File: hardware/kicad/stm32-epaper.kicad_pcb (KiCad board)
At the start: 4 copper layers, 97.4 x 60 mm, 155 parts, among them J1 USB_C_Receptacle_USB2.0_16P, J101 TC2050-IDC-NL, J102 UART (TX RX GND), J2 BATT (1S LiPo), J201 microSD, J301 IT8951 HAT, J302 Electrodes L, J303 Electrodes R, SW101 BOOT, SW301 PEC11R-4220F-S0024, SW302 POWER, U1 BQ24073RGT, U101 STM32F469IIT6, U2 TPS63802DLA, U201 IS42S16400J-6TLI, U202 W25Q128JVSIQ, U3 TPS61023DRL, U301 CAP1188-1-CP-TR, U302 TPD4E05U06DQAR, U4 TPS22965DSG, U5 USBLC6-2SC6, U6 TPS63900DSK, U7 MCP1700T-3002E/TT, Y101 8MHz CL8pF, Y102 32.768kHz CL6pF

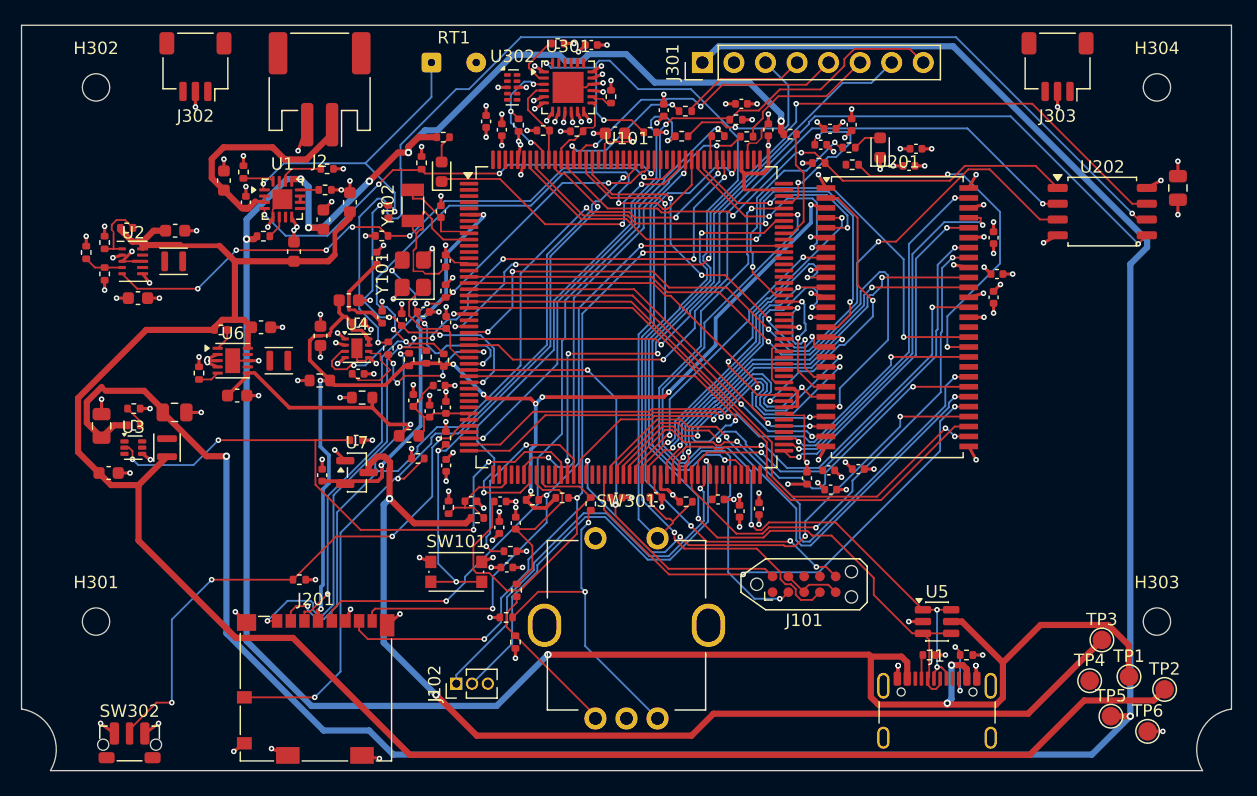
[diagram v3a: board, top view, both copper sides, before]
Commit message: Routing attempt 3: optimised placement (MCU 90 deg) -> 49 unconnected, QSPI 84->34 mm
Via spacing errors fixed. Persistent failures are the Power (0.5 mm) and
Touch (0.4 mm clearance) classes at 0.5 mm-pitch pins; crystals pushed
away by the decoupling caps.

Co-Authored-By: Claude Opus 5.5 <noreply@anthropic.com>
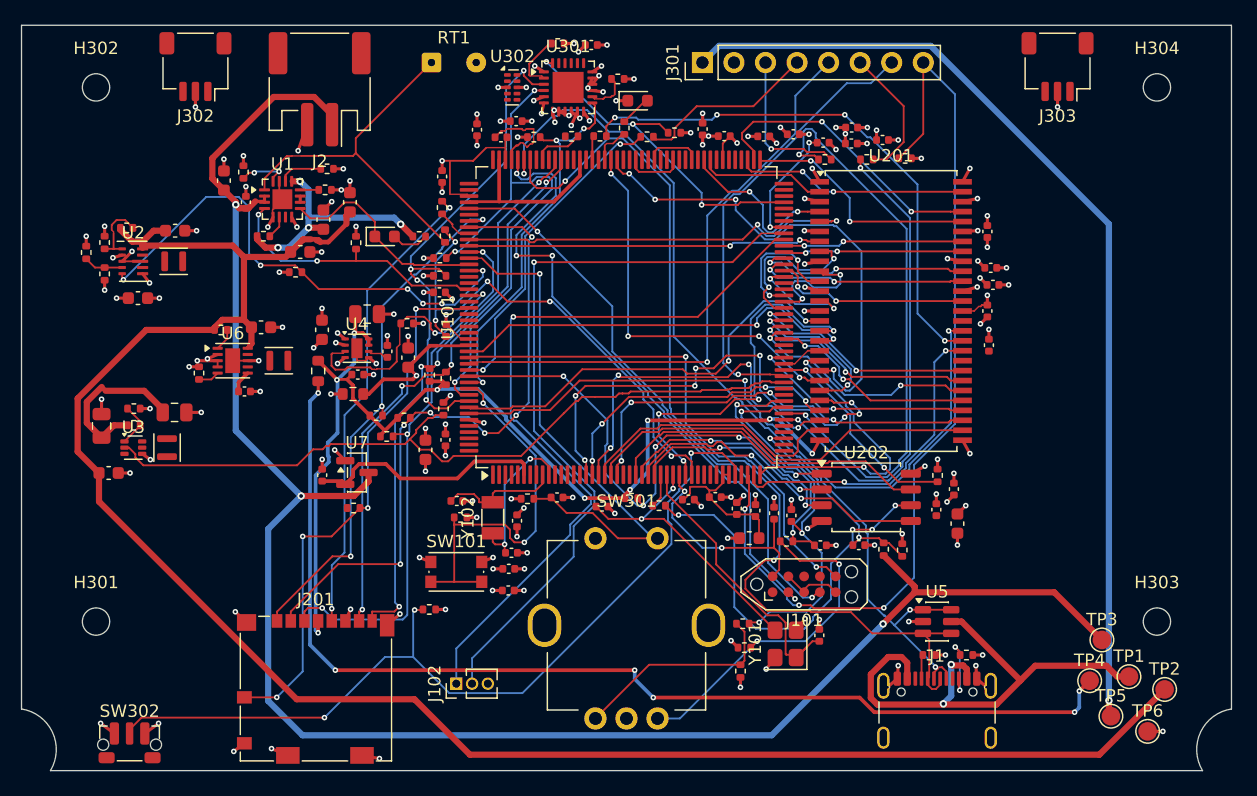
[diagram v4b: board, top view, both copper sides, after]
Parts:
- moved C208 66.0 mm to (127.8, 123.3), turned to 0 degrees
- moved C210 52.2 mm to (175.3, 140.1), turned to 90 degrees
- moved C105 42.7 mm to (177.9, 125.8), turned to 90 degrees
- moved Y101 42.3 mm to (161.5, 149.8)
- moved C122 39.2 mm to (164.2, 149.1)
- moved R22 36.7 mm to (170.9, 142.2)
- moved C104 35.2 mm to (173.6, 139.0)
- moved R102 34.9 mm to (173.7, 136.2), turned to 90 degrees
- moved R21 32.8 mm to (169.4, 142.2), turned to 90 degrees
- moved C17 31.4 mm to (167.4, 141.8)
- moved R201 30.9 mm to (149.1, 138.1)
- moved C106 30.6 mm to (162.1, 108.8), turned to 0 degrees
- moved C107 30.0 mm to (159.7, 108.9), turned to 0 degrees
- moved C120 29.9 mm to (164.5, 109.4)
- moved U202 29.8 mm to (168.0, 138.0)
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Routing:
- net VBUS: track 199.5 -> 63.0 mm, vias 9 -> 6
- net +5V: track 195.7 -> 92.4 mm, vias 2 -> 1
- net +3V3: track 8.64 -> 96.4 mm, vias 10 -> 15
- net QSPI_FLASH_CLK: track 92.2 -> 33.8 mm, vias 2 -> 4
- net QUADSPI_BK1_IO1: track 62.0 -> 16.3 mm
- net QUADSPI_BK1_IO0: track 70.4 -> 25.4 mm
- net QUADSPI_BK1_IO3: track 71.3 -> 26.4 mm, vias 4 -> 0
- net QUADSPI_BK1_IO2: track 63.4 -> 19.1 mm, vias 4 -> 2
- net +BATT: track 108.8 -> 149.3 mm, vias 2 -> 3
- net CAP_RESET: track 64.9 -> 28.2 mm
- net I2C1_SCL: track 7.26 -> 42.4 mm, vias 0 -> 3
- net FMC_BA0: track 9.41 -> 39.7 mm, vias 2 -> 4
- net I2C1_SDA: track 10.5 -> 40.5 mm, vias 3 -> 4
- net FMC_SDNRAS: track 30.9 -> 3.31 mm, vias 2 -> 0
- net SDIO_CMD: track 71.9 -> 44.4 mm, vias 4 -> 3
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
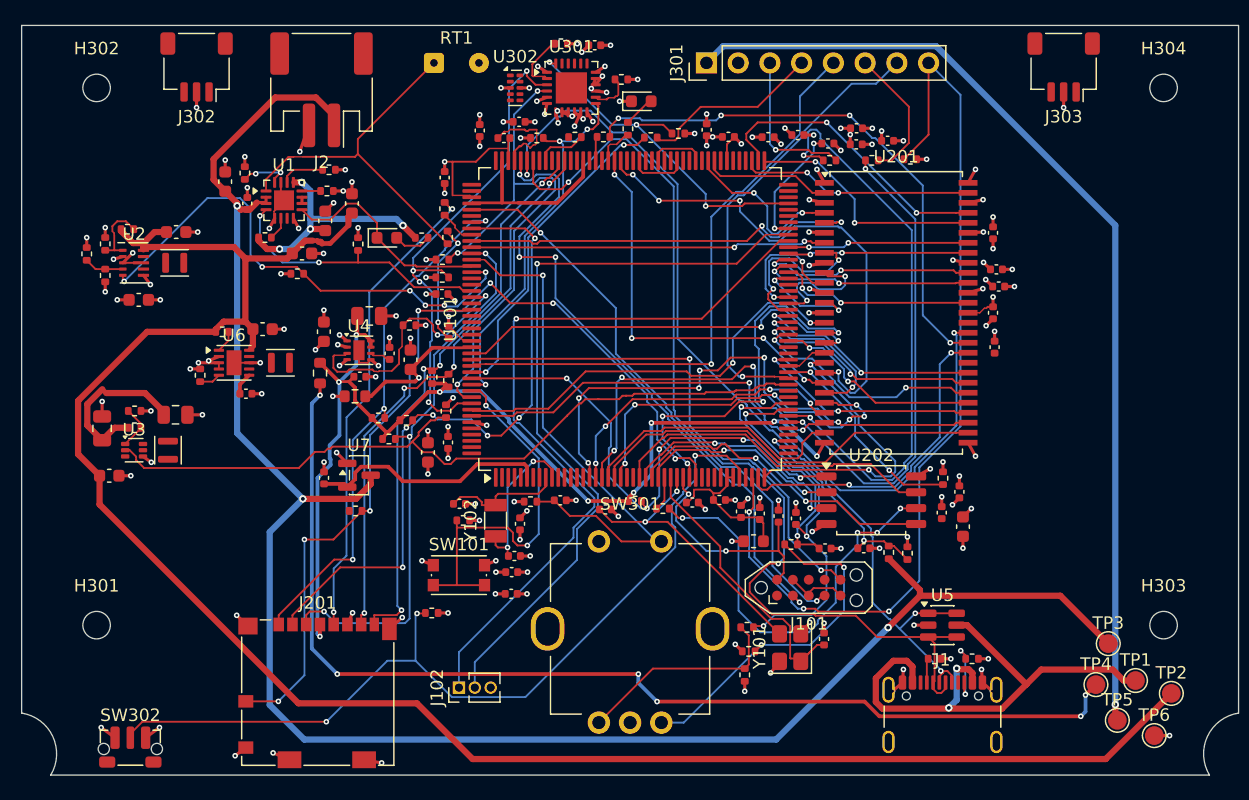
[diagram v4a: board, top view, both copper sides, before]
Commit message: Routing attempt 4: 35 unconnected / 7 nets (best so far)
Power class 0.3 mm (enters 0.5 mm-pitch pads), Touch clearance 0.25 mm,
crystals and clock resistors placed first; skew limits set from a
5%-of-period budget (SDRAM 30 mm, SDIO/QSPI 15 mm) instead of the
over-tight first draft.

Co-Authored-By: Claude Opus 5.5 <noreply@anthropic.com>
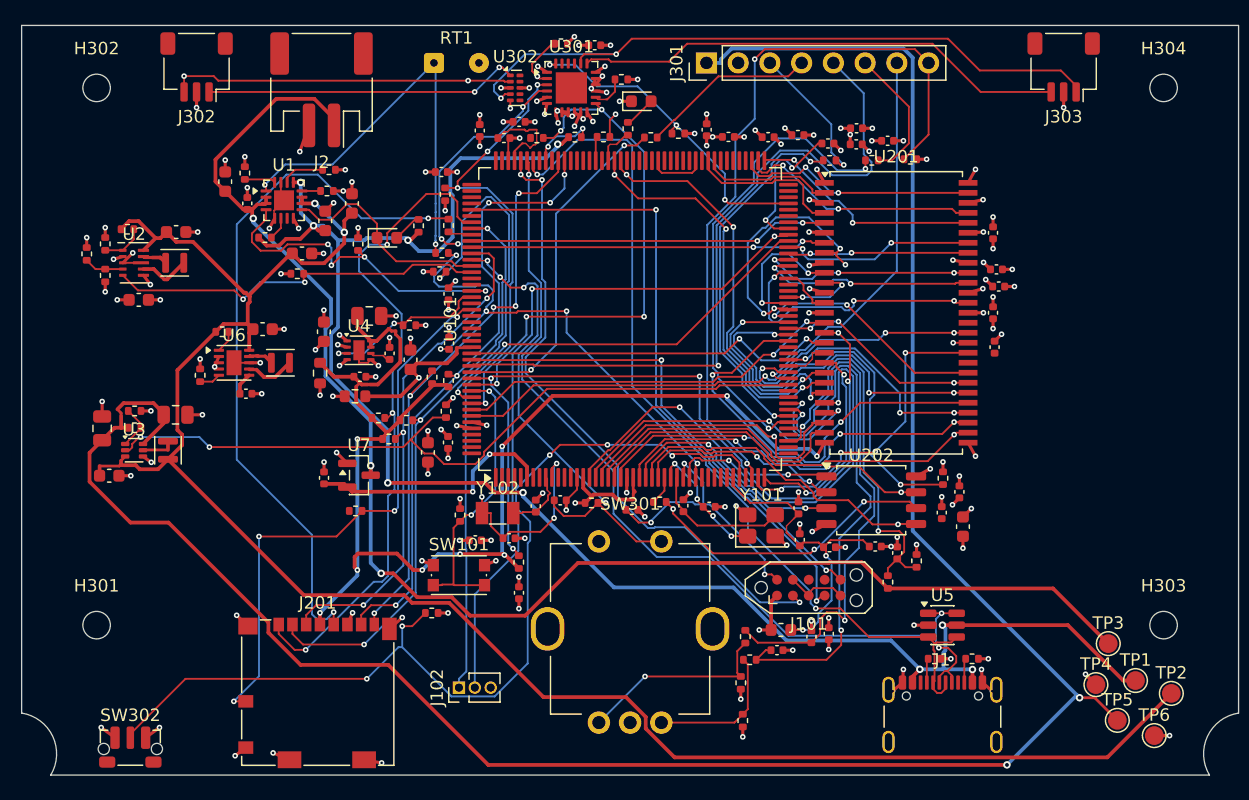
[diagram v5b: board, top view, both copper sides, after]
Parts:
- moved C103 26.2 mm to (164.6, 148.7)
- moved C118 15.1 mm to (168.3, 141.7)
- moved C122 14.0 mm to (155.0, 138.5), turned to 0 degrees
- moved C126 11.7 mm to (148.8, 138.8), turned to 0 degrees
- moved R201 10.5 mm to (139.8, 143.0), turned to 90 degrees
- moved Y101 10.0 mm to (159.2, 140.0), turned to 0 degrees
- moved R313 9.81 mm to (158.3, 150.8)
- moved C303 9.54 mm to (163.2, 148.9)
- moved C304 9.01 mm to (160.5, 150.0)
- moved FB101 7.43 mm to (160.8, 148.4)
- moved R305 6.65 mm to (133.9, 113.5), turned to 90 degrees
- moved C116 6.36 mm to (162.2, 138.6), turned to 90 degrees
- moved C123 6.24 mm to (153.0, 138.4), turned to 90 degrees
- moved C119 6.20 mm to (164.7, 141.8), turned to 0 degrees
- moved C124 6.11 mm to (141.1, 138.5), turned to 90 degrees
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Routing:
- net +5V: track 92.4 -> 184.4 mm, vias 1 -> 2
- net +3V3: track 96.4 -> 9.82 mm, vias 15 -> 11
- net VBUS: track 63.0 -> 138.8 mm, vias 6 -> 9
- net /Peripherals/TOUCH_R1: track 0.00 -> 55.8 mm, vias 0 -> 2
- net SDRAM_CLK: track 43.6 -> 3.20 mm, vias 4 -> 2
- net /Peripherals/TOUCH_R2: track 0.00 -> 40.2 mm, vias 0 -> 1
- net +BATT: track 149.3 -> 118.8 mm
- net /Peripherals/TOUCH_L2: track 0.00 -> 27.6 mm, vias 0 -> 2
- net /Peripherals/TOUCH_L1: track 0.00 -> 25.2 mm, vias 0 -> 2
- net ENC_B: track 20.4 -> 45.0 mm
- net SDCARD_CLK: track 38.0 -> 56.9 mm
- net GND: track 155.1 -> 137.2 mm, vias 128 -> 130
- net FMC_A7: track 16.8 -> 34.1 mm
- net SPI1_SCK: track 46.8 -> 29.6 mm
- net /Peripherals/ENC_B_RAW: track 28.0 -> 11.5 mm, vias 2 -> 0
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
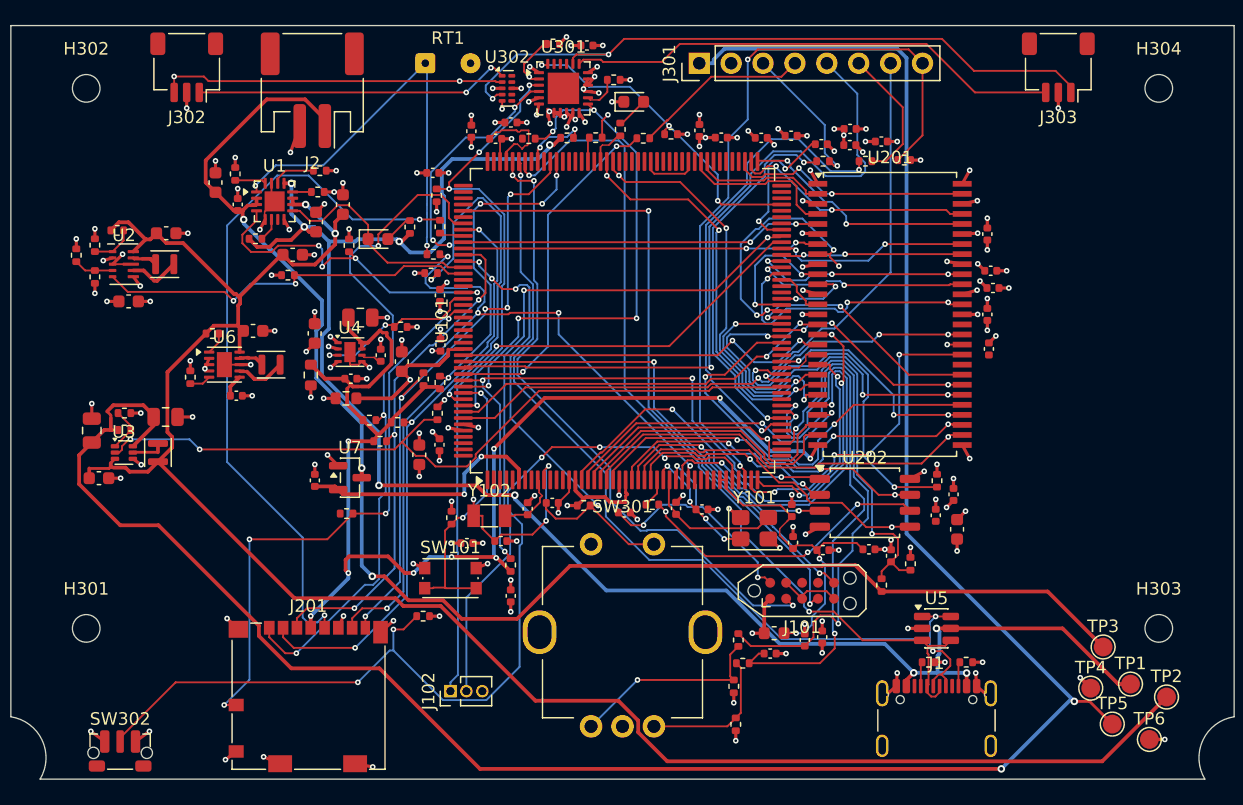
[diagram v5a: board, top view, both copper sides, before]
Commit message: Routing attempt 6: 31 unconnected / 6 nets - only 2 touch lines + plane-net pads open
Thermal-pad vias and pin-to-decoupling-cap stubs in the pre-router.

Co-Authored-By: Claude Opus 5.5 <noreply@anthropic.com>
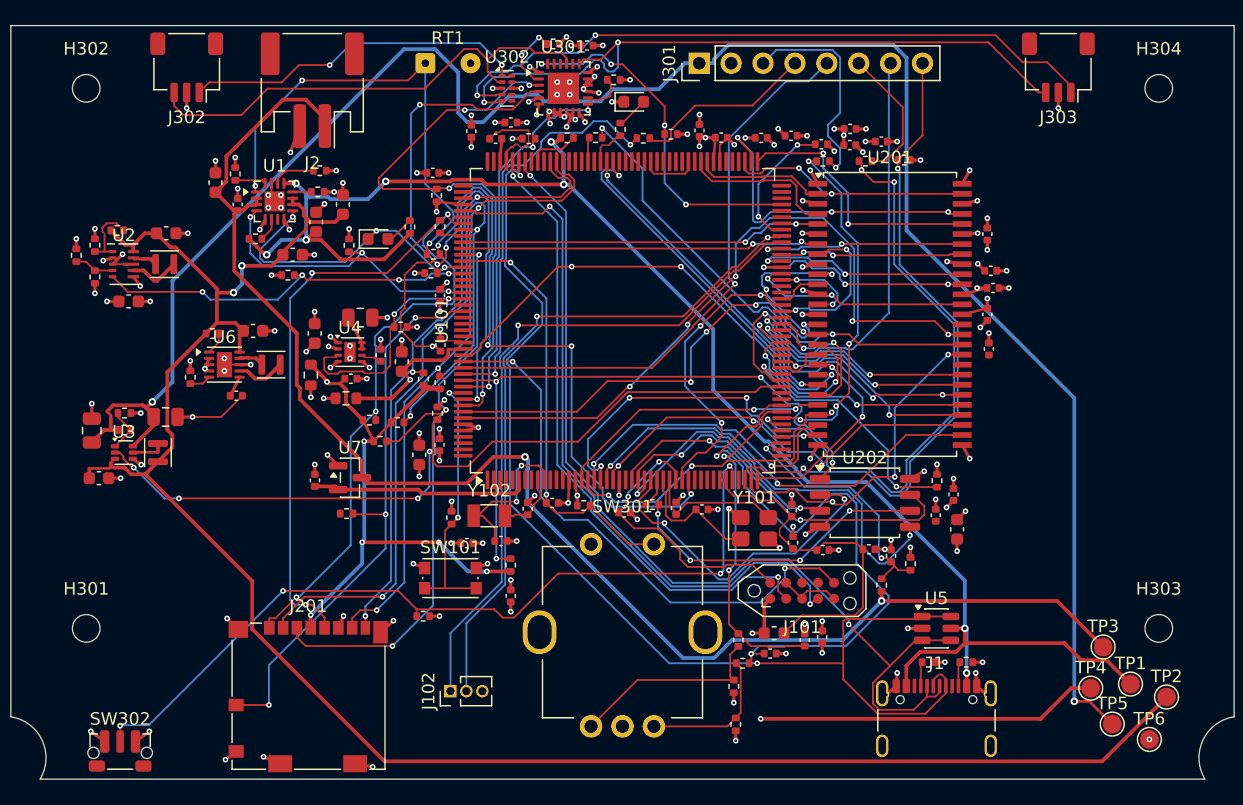
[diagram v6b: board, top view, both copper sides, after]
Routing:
- net 3V3_PERIPH: track 117.5 -> 74.4 mm, vias 25 -> 22
- net SDRAM_CLK: track 3.20 -> 39.0 mm
- net +5V: track 184.4 -> 157.0 mm
- net +3V3: track 9.82 -> 35.9 mm
- net TS_SENSE: track 40.4 -> 60.9 mm
- net FMC_A0: track 40.9 -> 21.8 mm
- net SDIO_D3: track 47.3 -> 65.9 mm
- net USB_DP: track 73.1 -> 89.4 mm, vias 3 -> 2
- net ENC_A: track 43.7 -> 27.4 mm
- net /Peripherals/TOUCH_R2: track 40.2 -> 56.5 mm, vias 1 -> 2
- net FMC_A7: track 34.1 -> 19.7 mm
- net SDCARD_CLK: track 56.9 -> 42.8 mm
- net FMC_NBL1: track 42.7 -> 55.5 mm, vias 3 -> 5
- net CAP_ALERT: track 42.6 -> 30.5 mm, vias 5 -> 3
- net VBAT_SENSE: track 32.1 -> 20.2 mm
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
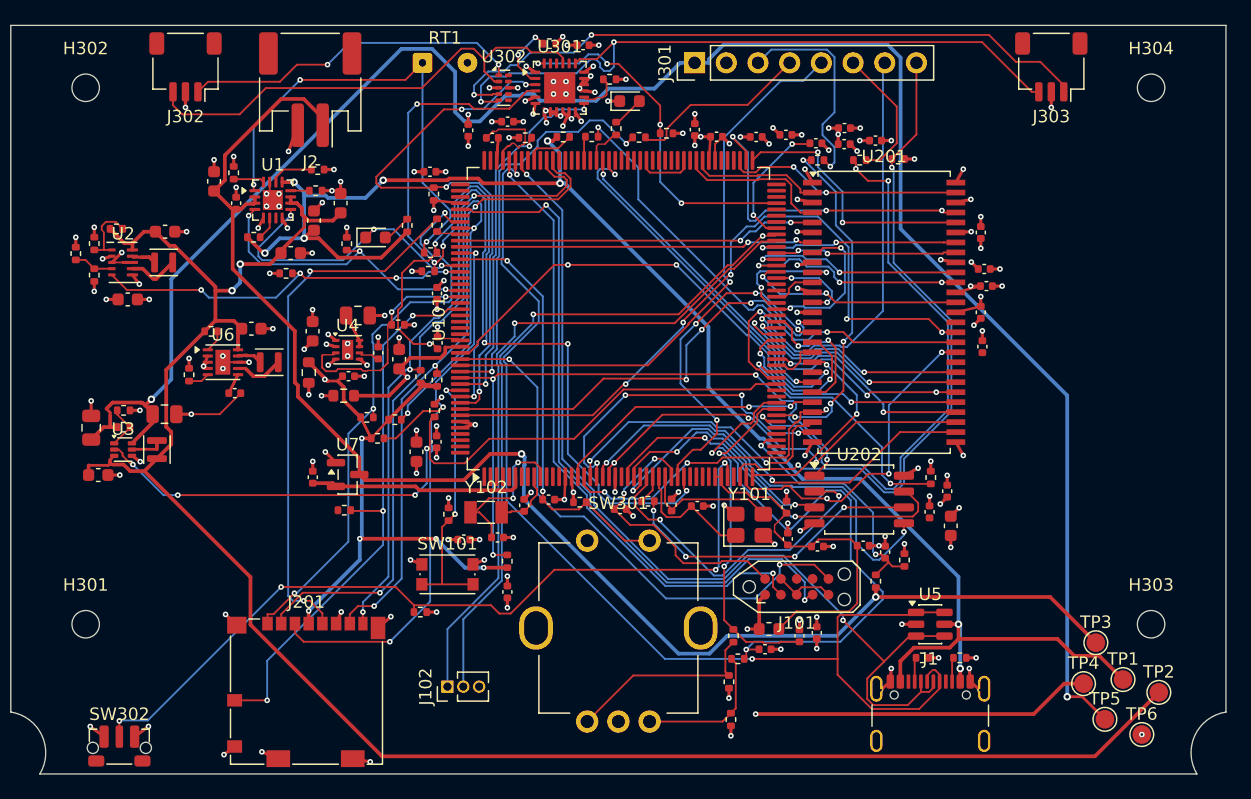
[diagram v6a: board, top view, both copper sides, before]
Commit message: Routing attempt 7: 29 unconnected / 4 nets (best)
Joined 3V3_PERIPH zone and test points at their rails fixed the long
+3V3/3V3_PERIPH gaps; inward MCU vias and CAP1188 escapes didn't take
(pre-router rejected them) - debugging next.

Co-Authored-By: Claude Opus 5.5 <noreply@anthropic.com>
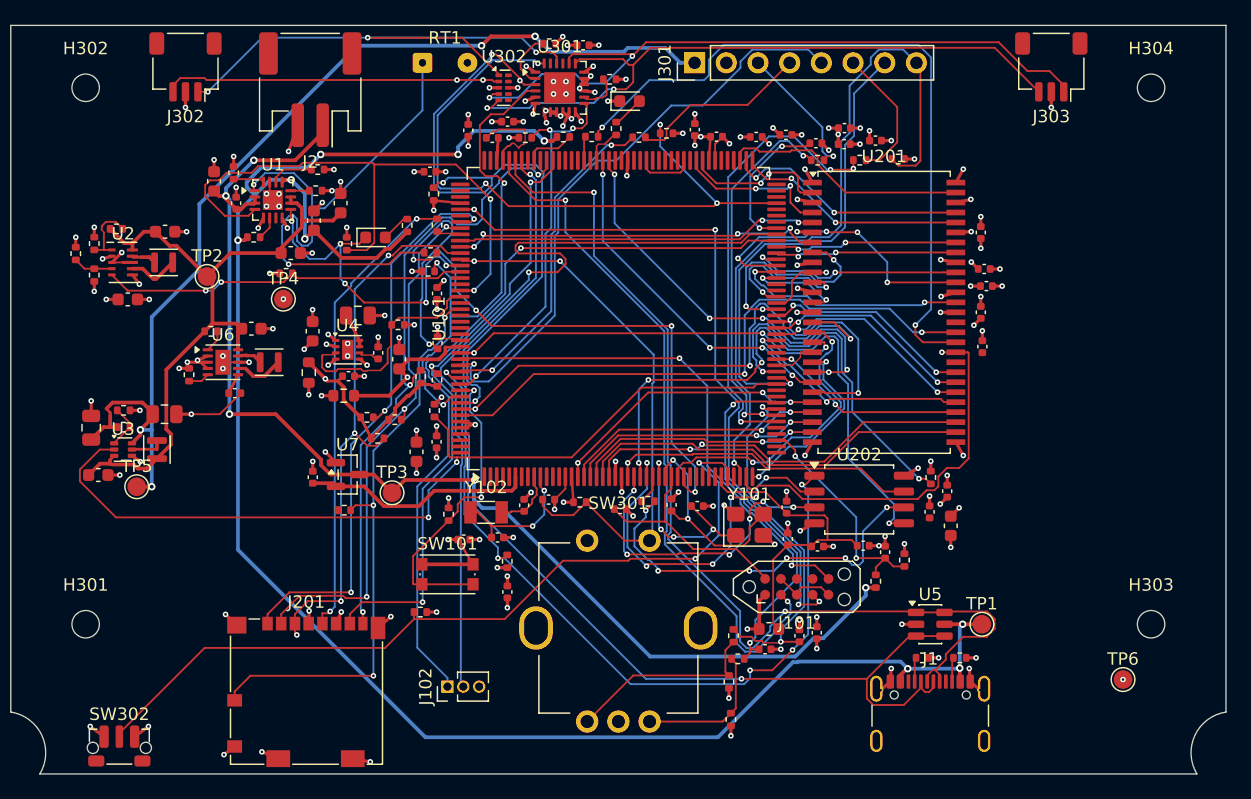
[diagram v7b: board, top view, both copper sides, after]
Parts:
- moved TP2 83.3 mm to (115.7, 120.1)
- moved TP5 79.8 mm to (110.1, 137.0)
- moved TP4 71.2 mm to (121.8, 121.9)
- moved TP3 57.7 mm to (130.6, 137.5)
- moved TP1 12.2 mm to (177.8, 148.0)
- moved TP6 4.66 mm to (189.2, 152.4)
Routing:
- net VSYS: track 151.4 -> 54.9 mm, vias 2 -> 0
- net +5V: track 157.0 -> 84.2 mm, vias 2 -> 4
- net 3V3_PERIPH: track 74.4 -> 43.7 mm, vias 22 -> 20
- net +3V3: track 35.9 -> 8.64 mm
- net VBUS: track 128.5 -> 154.1 mm, vias 8 -> 9
- net CHG_DIS: track 23.8 -> 48.2 mm, vias 3 -> 2
- net CAP_RESET: track 29.2 -> 53.3 mm
- net SDIO_D3: track 65.9 -> 43.2 mm
- net +BATT: track 117.2 -> 97.8 mm, vias 2 -> 5
- net SDRAM_CLK: track 39.0 -> 57.4 mm
- net ENC_B: track 47.2 -> 29.2 mm
- net /Peripherals/TOUCH_L1: track 27.3 -> 43.5 mm, vias 2 -> 3
- net QUADSPI_BK1_IO0: track 33.6 -> 46.4 mm, vias 2 -> 4
- net /MCU/USART3_RX: track 54.4 -> 66.6 mm, vias 2 -> 1
- net QUADSPI_BK1_NCS: track 51.3 -> 63.4 mm, vias 4 -> 5
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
